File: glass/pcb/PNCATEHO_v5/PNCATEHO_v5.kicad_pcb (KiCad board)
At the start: 2 copper layers, 97 x 59 mm, 27 parts, among them J1 TestPoint_2Pole, SW1 SW_PUSH, SW10 SW_PUSH, SW2 SW_PUSH, SW3 SW_PUSH, SW4 SW_PUSH, SW5 SW_PUSH, SW6 SW_PUSH, SW7 SW_PUSH, SW8 SW_PUSH, SW9 SW_PUSH, U1 ProMicro_r

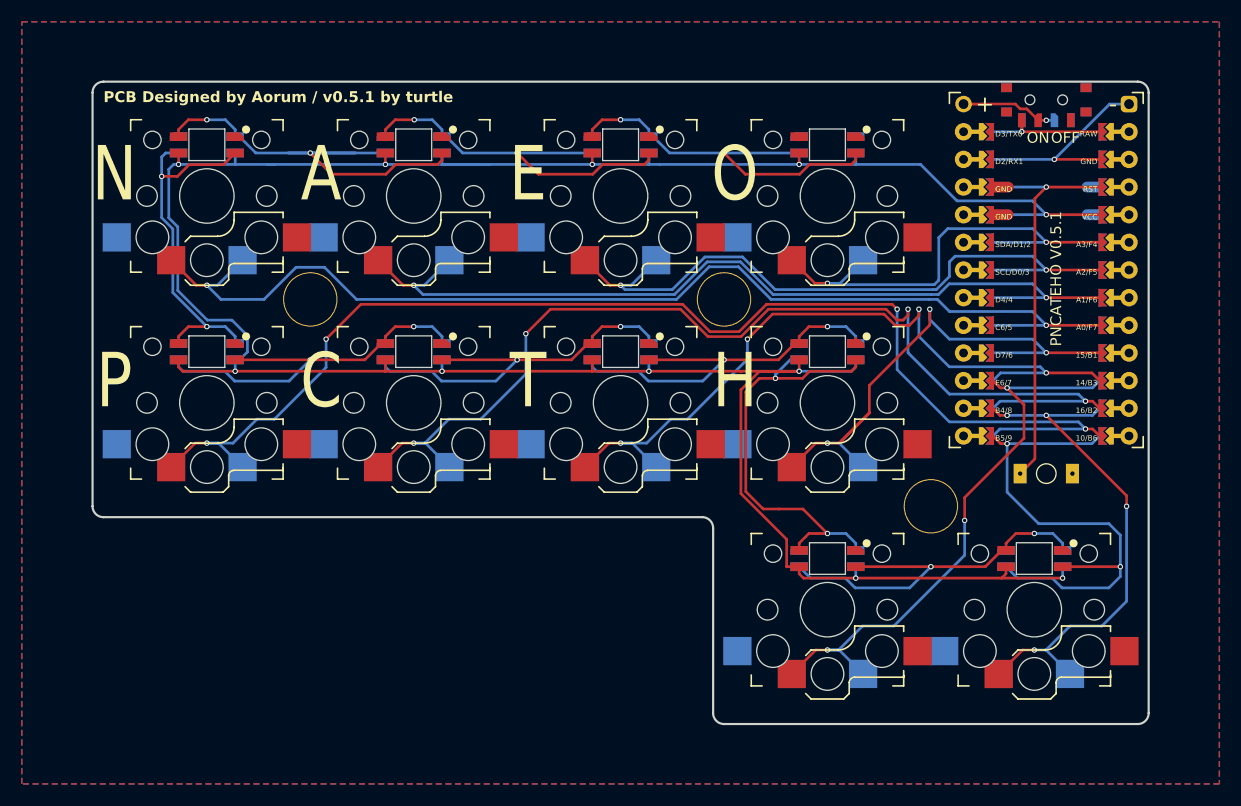
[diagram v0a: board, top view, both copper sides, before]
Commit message: Change led pin to TX0
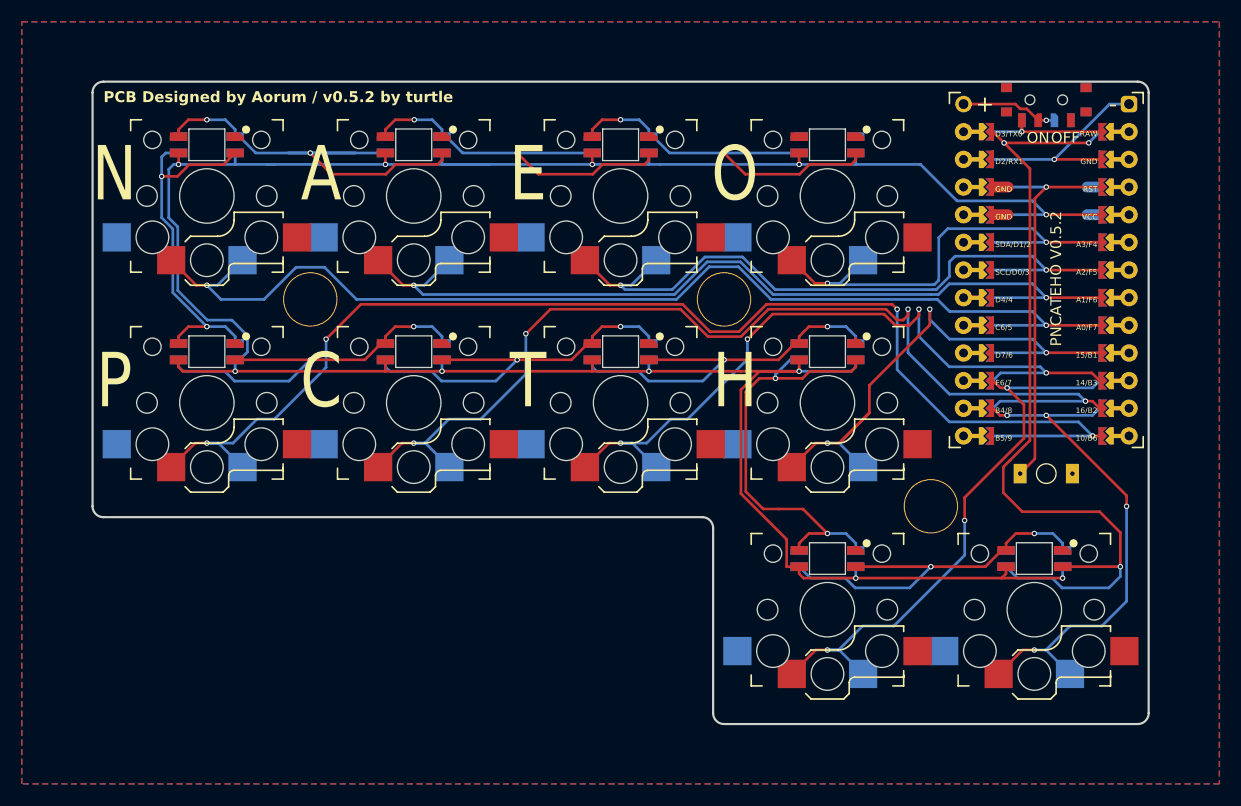
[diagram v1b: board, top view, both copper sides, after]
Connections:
- U1 pad 1: unconnected-(U1-D3/TX0-Pad1)_1 -> LED
- U1 pad 12: LED -> unconnected-(U1-B5/9-Pad12)
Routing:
- net LED: track 47.7 -> 78.1 mm, vias 2 -> 3
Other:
- board text added: "PCB Designed by Aorum / v0.5.2 by turtle"
- board text added: "PNCATEHO V0.5.2"
- board text removed: "PCB Designed by Aorum / v0.5.1 by turtle"
- board text removed: "PNCATEHO V0.5.1"
